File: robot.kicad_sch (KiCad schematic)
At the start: 44 parts, among them J1 PCA9865 2, J2 I2S, J3 Programming, J4 IMU, J5 Switches, J6 Expansion, SW1 Reset, SW2 Action, SW3 OPTION, SW4 Flash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

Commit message: Ready for fab.
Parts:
- added C1: 104, Capacitor_SMD:C_1206_3216Metric_Pad1.33x1.80mm_HandSolder, symbol Device:C
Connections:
- net GND: now also C1.1
- net VCC: now also C1.2

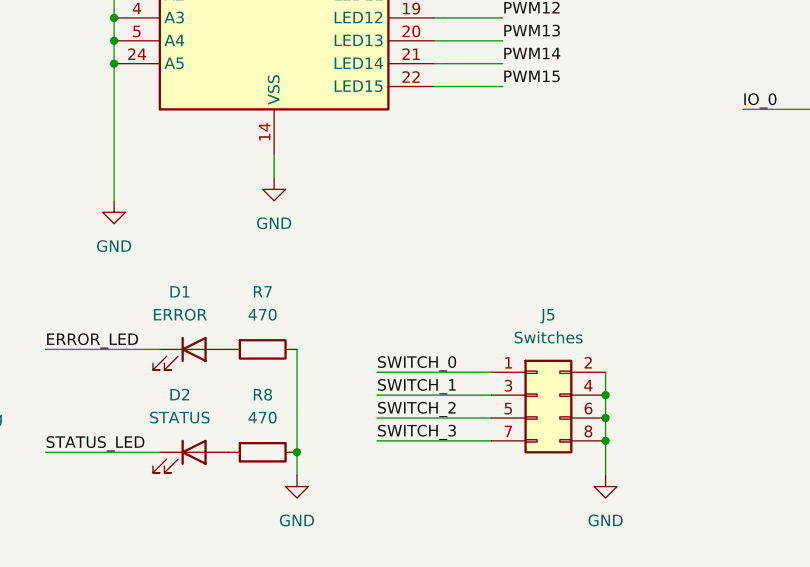
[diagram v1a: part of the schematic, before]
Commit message: Added minor footprint changes after trying to build the board. Added pin to switch battery to Vin.
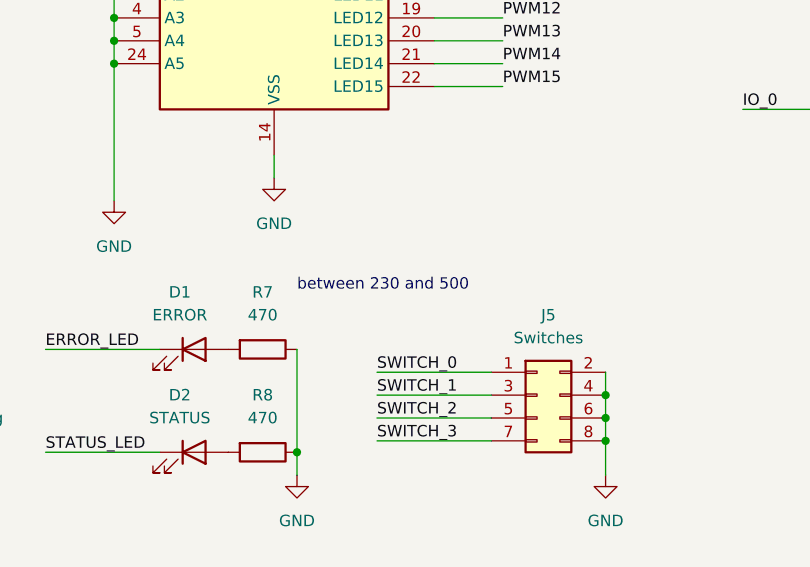
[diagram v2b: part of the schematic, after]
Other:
- note added: "between 230 and 500"
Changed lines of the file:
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@@
     (stroke (width 0) (type default) (color 0 0 0 0))
+  )
+  (text "between 230 and 500" (at 135.89 170.18 0)
+    (effects (font (size 1.27 1.27)) (justify left bottom))
   )
   (label "IO_34" (at 71.12 158.75 0)
@@
       (reference "J10") (unit 1) (value "BATT out") (footprint "Connector_PinHeader_2.54mm:Connector_Battery_SolderPads")
     )
+    (path "/78a56bae-3afa-4383-914f-3e74817e0e83/11aa9fda-6794-4a5a-9d23-47eb9aa4dd78"
+      (reference "J11") (unit 1) (value "Vin") (footprint "Connector_PinHeader_2.54mm:Connector_Battery_SolderPads")
+    )
     (path "/0a4a922c-7e89-4477-837a-33d7e39618b5"
       (reference "JP1") (unit 1) (value "HEADER-3X04") (footprint "Adafruit:3X04")
@@
     )
     (path "/78a56bae-3afa-4383-914f-3e74817e0e83/0f47f35a-e446-4771-a968-01260f35d28d"
-      (reference "SW5") (unit 1) (value "POWER") (footprint "Button_Switch_THT:SW_Slide_1P2T_CK_OS102011MS2Q")
+      (reference "SW5") (unit 1) (value "POWER") (footprint "KiCAD Custom Libs:Switch-SS12F23")
     )
     (path "/78a56bae-3afa-4383-914f-3e74817e0e83/5678e00d-7048-4a0a-a8c6-a9585d7c80a9"

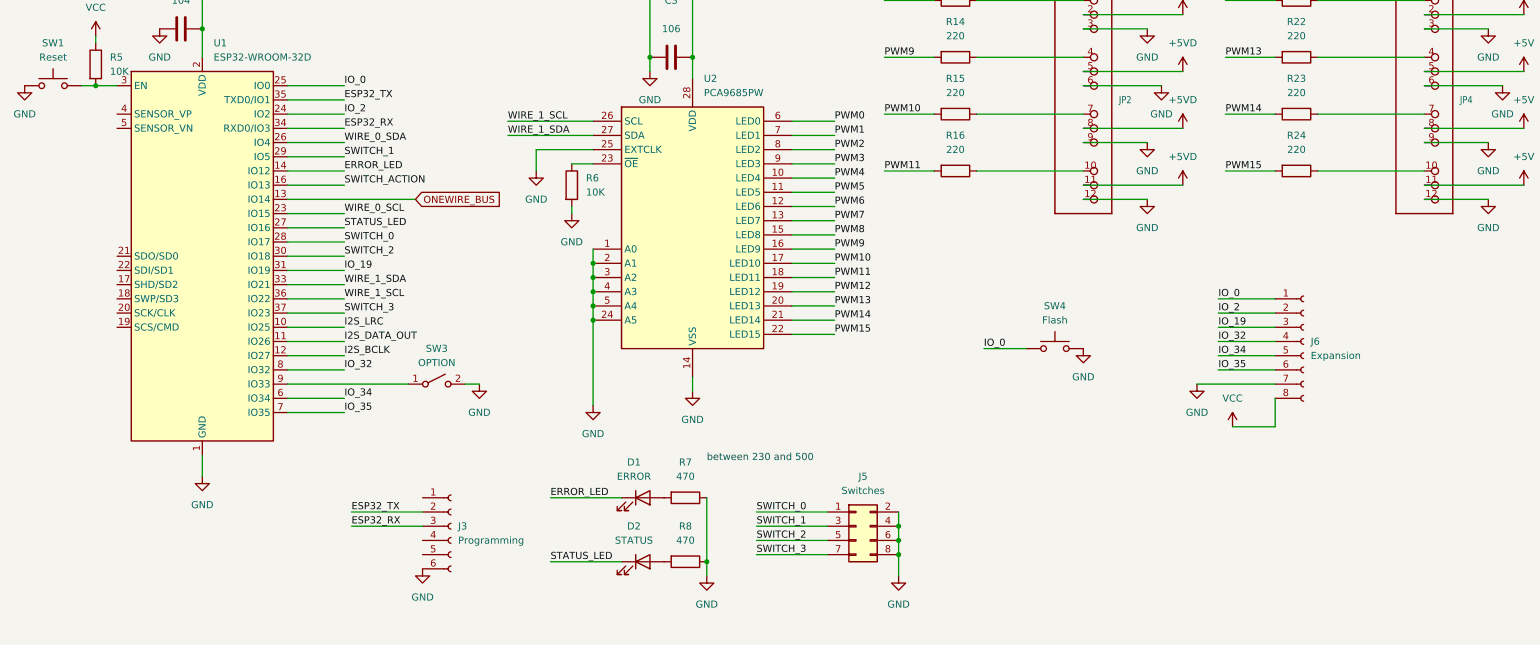
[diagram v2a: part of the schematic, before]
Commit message: Added extra pins and input from revision 1.
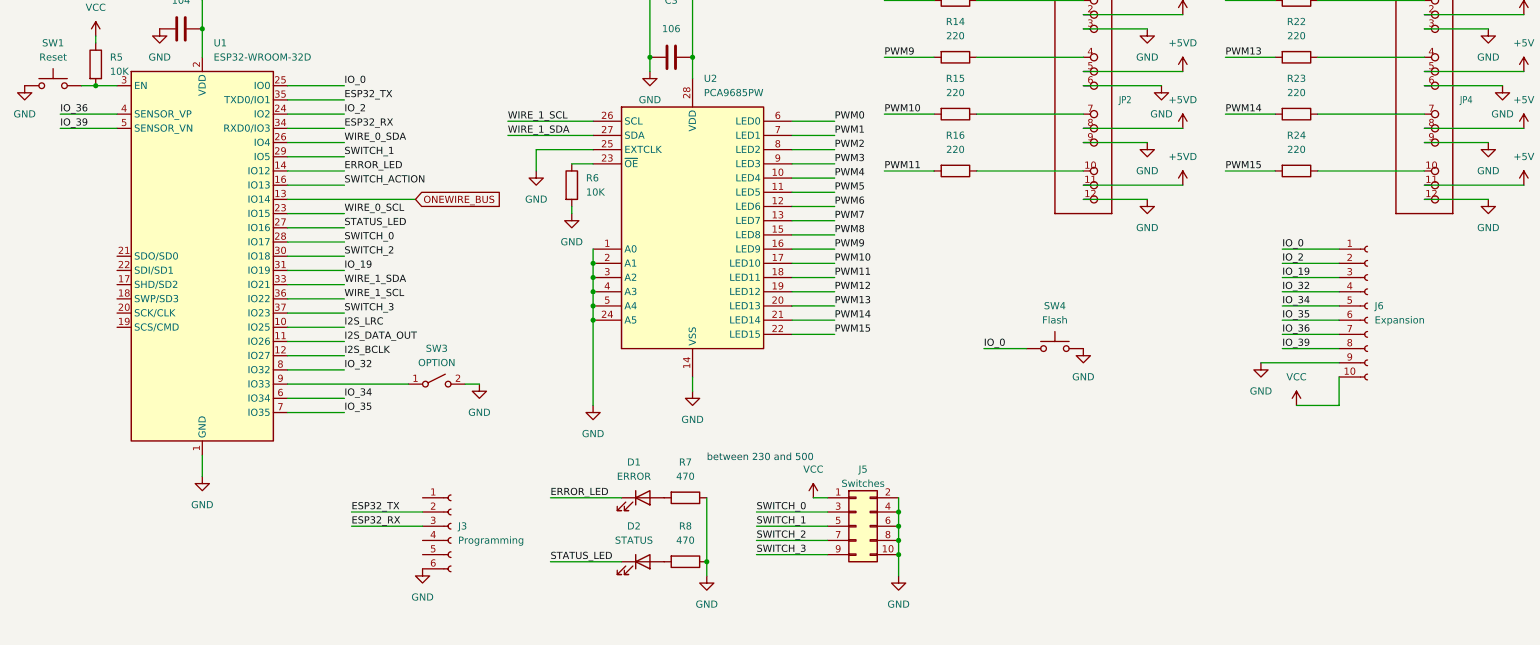
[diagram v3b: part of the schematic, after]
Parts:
- J5: symbol Connector_Generic:Conn_02x04_Odd_Even -> Connector_Generic:Conn_02x05_Odd_Even
- J6: footprint Connector_PinSocket_2.54mm:PinSocket_1x08_P2.54mm_Vertical -> Connector_PinSocket_2.54mm:PinSocket_1x10_P2.54mm_Vertical; symbol Connector:Conn_01x08_Female -> Connector:Conn_01x10_Female
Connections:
- net GND: now also J5.10 (Pin_10), J6.9 (Pin_9); no longer J6.7 (Pin_7)
- net SWITCH_0: now also J5.3 (Pin_3); no longer J5.1 (Pin_1)
- net SWITCH_1: now also J5.5 (Pin_5); no longer J5.3 (Pin_3)
- net SWITCH_2: now also J5.7 (Pin_7); no longer J5.5 (Pin_5)
- net SWITCH_3: now also J5.9 (Pin_9); no longer J5.7 (Pin_7)
- net VCC: now also J5.1 (Pin_1), J6.10 (Pin_10); no longer J6.8 (Pin_8)
- net IO_36: now reaches U1.4 (SENSOR_VP)
- net IO_36: now also J6.7 (Pin_7)
- net IO_39: now reaches U1.5 (SENSOR_VN)
- net IO_39: now also J6.8 (Pin_8)

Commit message: Added revision 2 features, not routed.
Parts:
- removed J1: PCA9865 2, Connector_PinSocket_2.54mm:PinSocket_1x06_P2.54mm_Vertical, symbol Connector:Conn_01x06_Female
- removed J2: I2S, Connector_PinSocket_2.54mm:PinSocket_1x07_P2.54mm_Vertical, symbol Connector:Conn_01x07_Female
- removed J4: IMU, Connector_PinSocket_2.54mm:PinSocket_1x08_P2.54mm_Vertical, symbol Connector:Conn_01x08_Female
- removed J6: Expansion, Connector_PinSocket_2.54mm:PinSocket_1x10_P2.54mm_Vertical, symbol Connector:Conn_01x10_Female
- added D3: INFO, LED_SMD:LED_1206_3216Metric_Pad1.42x1.75mm_HandSolder, symbol Device:LED
- added R28: 470, Resistor_SMD:R_1206_3216Metric_Pad1.30x1.75mm_HandSolder, symbol Device:R
- J5: footprint Connector_PinSocket_2.54mm:PinSocket_2x04_P2.54mm_Vertical -> Connector_PinSocket_2.54mm:PinSocket_2x07_P2.54mm_Vertical; symbol Connector_Generic:Conn_02x05_Odd_Even -> Connector_Generic:Conn_02x07_Odd_Even
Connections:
- net GND: now also J5.12 (Pin_12), R28.1
- net IO_19 renamed SWITCH_4
- net SWITCH_4: now also J5.11 (Pin_11)
- net IO_2 renamed SWITCH_5
- net SWITCH_5: now also J5.13 (Pin_13)
- net IO_32 renamed INFO_LED
- net INFO_LED: now also D3.1 (K)
- new net: D3.2 (A), R28.2
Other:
- added sheet Ports (ports.kicad_sch)
- note added: "LED resistors between 230 and 500"
- note removed: "between 230 and 500"
- moved on the sheet: D1, D2, R7, R8

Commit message: Board ready to go.
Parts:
- removed R10, R11, R12, R13, R14, R15, R16, R17, R18, R19, R20, R21, R22, R23, R24, R9: 220, Resistor_SMD:R_1206_3216Metric_Pad1.30x1.75mm_HandSolder, symbol Device:R
- added RN1: 220, symbol Device:R_Pack04
- added RN2, RN3, RN4: 220, Resistor_SMD:R_Array_Concave_4x0603, symbol Device:R_Pack04
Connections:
- net GND: now also J5.1 (Pin_1), J5.11 (Pin_11), J5.13 (Pin_13), J5.3 (Pin_3), J5.5 (Pin_5), J5.7 (Pin_7), J5.9 (Pin_9); no longer J5.10 (Pin_10), J5.12 (Pin_12), J5.2 (Pin_2), J5.4 (Pin_4), J5.6 (Pin_6), J5.8 (Pin_8)
- net PWM0: now also RN1.1 (R1.1)
- net PWM1: now also RN1.2 (R2.1)
- net PWM10: now also RN2.3 (R3.1)
- net PWM11: now also RN2.4 (R4.1)
- net PWM12: now also RN4.5 (R4.2)
- net PWM13: now also RN4.6 (R3.2)
- net PWM14: now also RN4.7 (R2.2)
- net PWM15: now also RN4.8 (R1.2)
- net PWM2: now also RN1.3 (R3.1)
- net PWM3: now also RN1.4 (R4.1)
- net PWM4: now also RN3.5 (R4.2)
- net PWM5: now also RN3.6 (R3.2)
- net PWM6: now also RN3.7 (R2.2)
- net PWM7: now also RN3.8 (R1.2)
- net PWM8: now also RN2.1 (R1.1)
- net PWM9: now also RN2.2 (R2.1)
- net SWITCH_0: now also J5.12 (Pin_12); no longer J5.3 (Pin_3)
- net SWITCH_1: now also J5.10 (Pin_10); no longer J5.5 (Pin_5)
- net SWITCH_2: now also J5.8 (Pin_8); no longer J5.7 (Pin_7)
- net SWITCH_3: now also J5.6 (Pin_6); no longer J5.9 (Pin_9)
- net SWITCH_4: now also J5.4 (Pin_4); no longer J5.11 (Pin_11)
- net SWITCH_5: now also J5.2 (Pin_2); no longer J5.13 (Pin_13)
- net VCC: now also J5.14 (Pin_14); no longer J5.1 (Pin_1)
- net at JP4.1: now also RN4.4 (R4.1)
- net at JP1.1: now also RN1.8 (R1.2)
- net at JP1.10: now also RN1.5 (R4.2)
- net at JP1.4: now also RN1.7 (R2.2)
- net at JP1.7: now also RN1.6 (R3.2)
- net at JP3.1: now also RN3.4 (R4.1)
- net at JP3.10: now also RN3.1 (R1.1)
- net at JP3.4: now also RN3.3 (R3.1)
- net at JP3.7: now also RN3.2 (R2.1)
- net at JP4.10: now also RN4.1 (R1.1)
- net at JP2.10: now also RN2.5 (R4.2)
- net at JP2.1: now also RN2.8 (R1.2)
- net at JP2.4: now also RN2.7 (R2.2)
- net at JP2.7: now also RN2.6 (R3.2)
- net at JP4.4: now also RN4.3 (R3.1)
- net at JP4.7: now also RN4.2 (R2.1)
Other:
- moved on the sheet: J5

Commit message: Clean chematic
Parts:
- removed C2: 104, Capacitor_SMD:C_1206_3216Metric_Pad1.33x1.80mm_HandSolder, symbol Device:C
- removed C3: 106, Capacitor_SMD:C_1210_3225Metric_Pad1.33x2.70mm_HandSolder, symbol Device:C
- removed JP1, JP2, JP3, JP4: HEADER-3X04, Adafruit:3X04, symbol Adafruit:HEADER-3X04
- removed R6: 10K, Resistor_SMD:R_1206_3216Metric_Pad1.30x1.75mm_HandSolder, symbol Device:R
- removed RN1: 220, symbol Device:R_Pack04
- removed RN2, RN3, RN4: 220, Resistor_SMD:R_Array_Concave_4x0603, symbol Device:R_Pack04
- removed U2: PCA9685PW, Package_SO:TSSOP-28_4.4x9.7mm_P0.65mm, symbol Driver_LED:PCA9685PW
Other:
- added sheet servos (servos.kicad_sch)
- moved on the sheet: SW4

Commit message: Very minor tweaks for board version 3.
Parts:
- added R10: 10K, Resistor_SMD:R_1206_3216Metric_Pad1.30x1.75mm_HandSolder, symbol Device:R
- added SW6: OPTION, Button_Switch_SMD:SW_SPST_CK_RS282G05A3, symbol Switch:SW_Push
- SW3: value OPTION -> KILL
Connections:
- net GND: now also SW6.2
- net IO_34: now also R10.1, SW6.1
- net VCC: now also R10.2
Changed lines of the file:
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@@
   (junction (at 170.18 176.53) (diameter 0) (color 0 0 0 0)
   )
+  (junction (at 139.065 120.65) (diameter 0) (color 0 0 0 0)
+  )
   (junction (at 170.18 181.61) (diameter 0) (color 0 0 0 0)
   )
@@
   (junction (at 26.67 102.87) (diameter 0) (color 0 0 0 0)
   )
+  (wire (pts (xy 132.715 120.65) (xy 139.065 120.65))
+    (stroke (width 0) (type default) (color 0 0 0 0))
+  )
   (wire (pts (xy 152.4 173.99) (xy 157.48 173.99))
     (stroke (width 0) (type default) (color 0 0 0 0))
@@
     (stroke (width 0) (type default) (color 0 0 0 0))
   )
+  (wire (pts (xy 139.065 97.79) (xy 139.065 102.235))
+    (stroke (width 0) (type default) (color 0 0 0 0))
+  )
   (wire (pts (xy 50.8 69.85) (xy 53.34 69.85))
     (stroke (width 0) (type default) (color 0 0 0 0))
@@
     (stroke (width 0) (type default) (color 0 0 0 0))
   )
+  (wire (pts (xy 139.065 120.65) (xy 140.335 120.65))
+    (stroke (width 0) (type default) (color 0 0 0 0))
+  )
   (wire (pts (xy 60.96 113.03) (xy 71.12 113.03))
     (stroke (width 0) (type default) (color 0 0 0 0))
@@
     (stroke (width 0) (type default) (color 0 0 0 0))
   )
+  (wire (pts (xy 139.065 109.855) (xy 139.065 120.65))
+    (stroke (width 0) (type default) (color 0 0 0 0))
+  )
   (wire (pts (xy 17.78 187.96) (xy 25.4 187.96))
     (stroke (width 0) (type default) (color 0 0 0 0))
@@
   )
   (label "SWITCH_ACTION" (at 25.4 69.85 0)
+    (effects (font (size 1.27 1.27)) (justify left bottom))
+  )
+  (label "IO_34" (at 132.715 120.65 0)
     (effects (font (size 1.27 1.27)) (justify left bottom))
   )
@@
     (in_bom yes) (on_board yes) (fields_autoplaced)
     (property "Reference" "SW3" (id 0) (at 87.63 149.86 0))
-    (property "Value" "OPTION" (id 1) (at 87.63 152.4 0))
+    (property "Value" "KILL" (id 1) (at 87.63 152.4 0))
     (property "Footprint" "Button_Switch_THT:SW_Slide_1P2T_CK_OS102011MS2Q" (id 2) (at 87.63 156.21 0)
       (effects (font (size 1.27 1.27)) hide)
@@
     (pin "1")
     (pin "2")
+  )
+  (symbol (lib_id "power:VCC") (at 139.065 97.79 0) (unit 1)
+    (in_bom yes) (on_board yes) (fields_autoplaced)
+    (property "Reference" "#PWR0180" (id 0) (at 139.065 101.6 0)
+      (effects (font (size 1.27 1.27)) hide)
+    )
+    (property "Value" "VCC" (id 1) (at 139.065 92.71 0))
+    (property "Footprint" "" (id 2) (at 139.065 97.79 0)
+      (effects (font (size 1.27 1.27)) hide)
+    )
+    (property "Datasheet" "" (id 3) (at 139.065 97.79 0)
+      (effects (font (size 1.27 1.27)) hide)
+    )
+    (pin "1")
   )
   (symbol (lib_id "Device:R") (at 99.06 43.18 270) (unit 1)
@@
     )
     (property "Datasheet" "~" (id 3) (at 26.67 99.06 0)
+      (effects (font (size 1.27 1.27)) hide)
+    )
+    (pin "1")
+    (pin "2")
+  )
+  (symbol (lib_id "Switch:SW_Push") (at 145.415 120.65 0) (unit 1)
+    (in_bom yes) (on_board yes) (fields_autoplaced)
+    (property "Reference" "SW6" (id 0) (at 145.415 113.03 0))
+    (property "Value" "OPTION" (id 1) (at 145.415 115.57 0))
+    (property "Footprint" "Button_Switch_SMD:SW_SPST_CK_RS282G05A3" (id 2) (at 145.415 115.57 0)
+      (effects (font (size 1.27 1.27)) hide)
+    )
+    (property "Datasheet" "~" (id 3) (at 145.415 115.57 0)
       (effects (font (size 1.27 1.27)) hide)
     )
@@
     (pin "2")
   )
+  (symbol (lib_id "Device:R") (at 139.065 106.045 180) (unit 1)
+    (in_bom yes) (on_board yes) (fields_autoplaced)
+    (property "Reference" "R10" (id 0) (at 141.605 104.7749 0)
+      (effects (font (size 1.27 1.27)) (justify right))
+    )
+    (property "Value" "10K" (id 1) (at 141.605 107.3149 0)
+      (effects (font (size 1.27 1.27)) (justify right))
+    )
+    (property "Footprint" "Resistor_SMD:R_1206_3216Metric_Pad1.30x1.75mm_HandSolder" (id 2) (at 140.843 106.045 90)
+      (effects (font (size 1.27 1.27)) hide)
+    )
+    (property "Datasheet" "~" (id 3) (at 139.065 106.045 0)
+      (effects (font (size 1.27 1.27)) hide)
+    )
+    (pin "1")
+    (pin "2")
+  )
+  (symbol (lib_id "power:GND") (at 150.495 120.65 0) (unit 1)
+    (in_bom yes) (on_board yes) (fields_autoplaced)
+    (property "Reference" "#PWR0181" (id 0) (at 150.495 127 0)
+      (effects (font (size 1.27 1.27)) hide)
+    )
+    (property "Value" "GND" (id 1) (at 150.495 125.73 0))
+    (property "Footprint" "" (id 2) (at 150.495 120.65 0)
+      (effects (font (size 1.27 1.27)) hide)
+    )
+    (property "Datasheet" "" (id 3) (at 150.495 120.65 0)
+      (effects (font (size 1.27 1.27)) hide)
+    )
+    (pin "1")
+  )
   (symbol (lib_id "Device:C") (at 41.91 92.71 90) (unit 1)
     (in_bom yes) (on_board yes) (fields_autoplaced)
@@
       (reference "#PWR0179") (unit 1) (value "GND") (footprint "")
     )
+    (path "/2678ee08-149b-49de-a54f-df7e56cbe68b"
+      (reference "#PWR0180") (unit 1) (value "VCC") (footprint "")
+    )
+    (path "/d8a7a384-f511-452d-93bf-82ad3b87dfca"
+      (reference "#PWR0181") (unit 1) (value "GND") (footprint "")
+    )
     (path "/69ddaad4-6a4d-496c-81a2-3d2ec8ddf76d/8e06de31-fc7e-44ea-97d3-7e03c7b41eb6"
       (reference "#PWR0182") (unit 1) (value "GND") (footprint "")
@@
       (reference "#PWR0183") (unit 1) (value "GND") (footprint "")
     )
+    (path "/78a56bae-3afa-4383-914f-3e74817e0e83/9385543e-5933-4ff5-ba09-a2a4f0fdca05"
+      (reference "#PWR0184") (unit 1) (value "GND") (footprint "")
+    )
     (path "/69ddaad4-6a4d-496c-81a2-3d2ec8ddf76d/9d481041-2881-425a-8675-d600b5696326"
       (reference "#PWR0185") (unit 1) (value "GND") (footprint "")
@@
       (reference "#PWR0186") (unit 1) (value "GND") (footprint "")
     )
+    (path "/69ddaad4-6a4d-496c-81a2-3d2ec8ddf76d/c3e6618c-274f-488d-ad5e-ff1af3cdad3d"
+      (reference "#PWR0187") (unit 1) (value "+5VD") (footprint "")
+    )
+    (path "/69ddaad4-6a4d-496c-81a2-3d2ec8ddf76d/c6264c16-d938-4921-9b9d-3fded843f884"
+      (reference "#PWR0188") (unit 1) (value "+5V") (footprint "")
+    )
     (path "/69ddaad4-6a4d-496c-81a2-3d2ec8ddf76d/c1585d4f-11a0-49dc-afe5-0d1819d64bc6"
       (reference "#PWR0189") (unit 1) (value "GND") (footprint "")
@@
       (reference "#PWR0190") (unit 1) (value "GND") (footprint "")
     )
+    (path "/69ddaad4-6a4d-496c-81a2-3d2ec8ddf76d/cacb4663-4148-4fed-a80a-131111e50b42"
+      (reference "#PWR0191") (unit 1) (value "+5VL") (footprint "")
+    )
     (path "/69ddaad4-6a4d-496c-81a2-3d2ec8ddf76d/4810aa35-94da-442f-8506-52567fa1d5af"
       (reference "#PWR0192") (unit 1) (value "VCC") (footprint "")
     )
+    (path "/69ddaad4-6a4d-496c-81a2-3d2ec8ddf76d/2edcaac3-e515-4919-9894-790049e27c17"
+      (reference "#PWR0193") (unit 1) (value "+5VA") (footprint "")
+    )
+    (path "/69ddaad4-6a4d-496c-81a2-3d2ec8ddf76d/05dd64f8-fec9-46fb-81a8-a98be524d42d"
+      (reference "#PWR0194") (unit 1) (value "GND") (footprint "")
+    )
     (path "/db11b079-8bb6-4dd3-9471-bf8f532970a8"
       (reference "C1") (unit 1) (value "104") (footprint "Capacitor_SMD:C_1206_3216Metric_Pad1.33x1.80mm_HandSolder")
@@
       (reference "C14") (unit 1) (value "106") (footprint "Capacitor_SMD:C_1210_3225Metric_Pad1.33x2.70mm_HandSolder")
     )
+    (path "/69ddaad4-6a4d-496c-81a2-3d2ec8ddf76d/9eb547e1-94f8-4de9-a520-7e0c694bcb99"
+      (reference "C15") (unit 1) (value "104") (footprint "Capacitor_SMD:C_1206_3216Metric_Pad1.33x1.80mm_HandSolder")
+    )
+    (path "/69ddaad4-6a4d-496c-81a2-3d2ec8ddf76d/892955cc-ff05-43ff-935e-192a9b6d877b"
+      (reference "C16") (unit 1) (value "104") (footprint "Capacitor_SMD:C_1206_3216Metric_Pad1.33x1.80mm_HandSolder")
+    )
+    (path "/69ddaad4-6a4d-496c-81a2-3d2ec8ddf76d/a621deda-3883-4030-b2c7-0bcf9546f630"
+      (reference "C17") (unit 1) (value "104") (footprint "Capacitor_SMD:C_1206_3216Metric_Pad1.33x1.80mm_HandSolder")
+    )
+    (path "/69ddaad4-6a4d-496c-81a2-3d2ec8ddf76d/8d216f60-1227-4496-95f5-123ac497a991"
+      (reference "C18") (unit 1) (value "104") (footprint "Capacitor_SMD:C_1206_3216Metric_Pad1.33x1.80mm_HandSolder")
+    )
     (path "/a4aef3bd-aa2d-4904-95d8-68b395f8e759"
       (reference "D1") (unit 1) (value "ERROR") (footprint "LED_SMD:LED_1206_3216Metric_Pad1.42x1.75mm_HandSolder")
@@
       (reference "R9") (unit 1) (value "10K") (footprint "Resistor_SMD:R_1206_3216Metric_Pad1.30x1.75mm_HandSolder")
     )
+    (path "/c8620253-9b8a-4b4c-81d1-d40b33b428a7"
+      (reference "R10") (unit 1) (value "10K") (footprint "Resistor_SMD:R_1206_3216Metric_Pad1.30x1.75mm_HandSolder")
+    )
+    (path "/e5978b14-44ae-4b29-b1cb-9f6153659d99/c3150ac7-822e-40b6-93b4-faffb3dee63c"
+      (reference "R11") (unit 1) (value "100K") (footprint "Resistor_SMD:R_1206_3216Metric_Pad1.30x1.75mm_HandSolder")
+    )
     (path "/78a56bae-3afa-4383-914f-3e74817e0e83/17bfc741-d0c7-4bef-87ee-616f2b4df88b"
-      (reference "R25") (unit 1) (value "SHUNT") (footprint "Resistor_SMD:R_1206_3216Metric_Pad1.30x1.75mm_HandSolder")
+      (reference "R25") (unit 1) (value "SHUNT") (footprint "Resistor_SMD:R_1812_4532Metric_Pad1.30x3.40mm_HandSolder")
     )
     (path "/78a56bae-3afa-4383-914f-3e74817e0e83/d254204e-5168-4bfd-b23c-f9a348b9ad4d"
@@
     )
     (path "/18a0cd10-e2df-4a45-8f26-c8ed85eca444"
-      (reference "SW3") (unit 1) (value "OPTION") (footprint "Button_Switch_THT:SW_Slide_1P2T_CK_OS102011MS2Q")
+      (reference "SW3") (unit 1) (value "KILL") (footprint "Button_Switch_THT:SW_Slide_1P2T_CK_OS102011MS2Q")
     )
     (path "/bf68c54e-5dad-4d99-bee2-d4cf8aed3ded"
@@
       (reference "SW5") (unit 1) (value "POWER") (footprint "KiCAD Custom Libs:Switch-SS12F23")
     )
+    (path "/61704a6f-c44d-4129-b66f-65b675e9f646"
+      (reference "SW6") (unit 1) (value "OPTION") (footprint "Button_Switch_SMD:SW_SPST_CK_RS282G05A3")
+    )
     (path "/78a56bae-3afa-4383-914f-3e74817e0e83/5678e00d-7048-4a0a-a8c6-a9585d7c80a9"
